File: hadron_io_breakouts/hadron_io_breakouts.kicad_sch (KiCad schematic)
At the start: 15 parts, among them J1 TF38-18S-0.5SV_830_, J2 SFM-110-02-L-D-A, J3 TF38-18S-0.5SV_830_, J4 SAMTEC-SFM-120-02-L-D-A, J5 SM04B-NSHSS-TB_LF__SN_, J6 SM08B-NSHSS-TB LFSN, J7 Conn_01x03_Pin

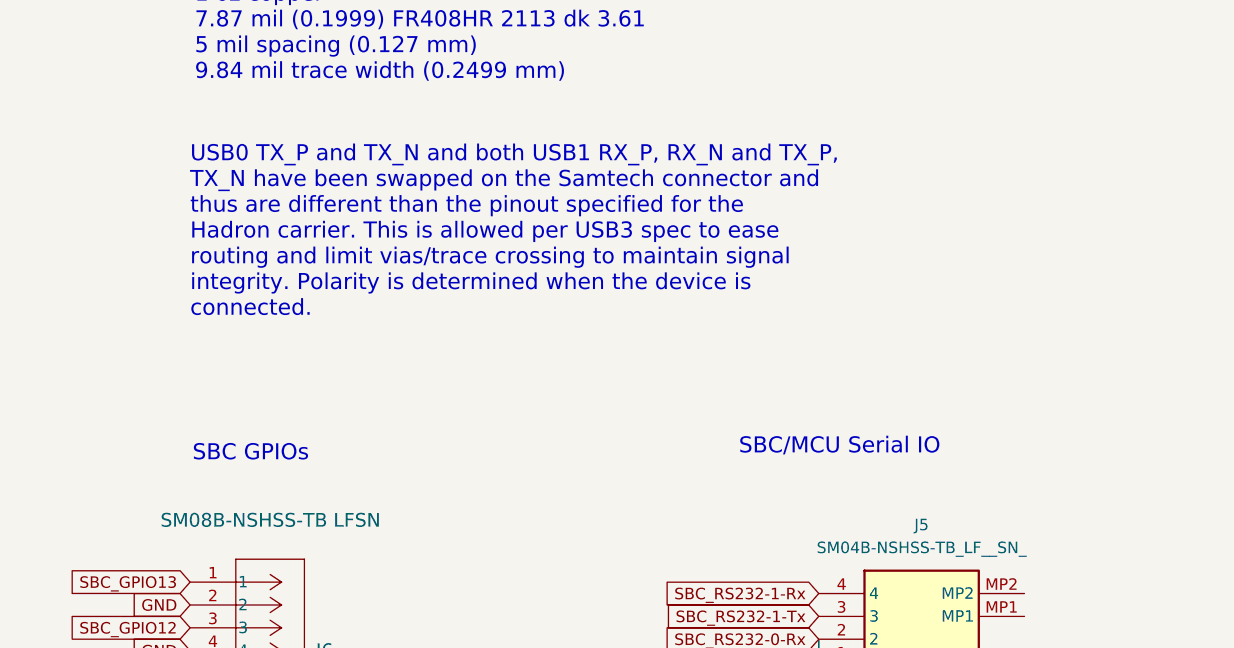
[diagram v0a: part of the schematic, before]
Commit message: added external trigger code to CamtrawlControl.ino
Minor cleanup of hadron_io_breakouts. Removed 6 layer version of the breakout.
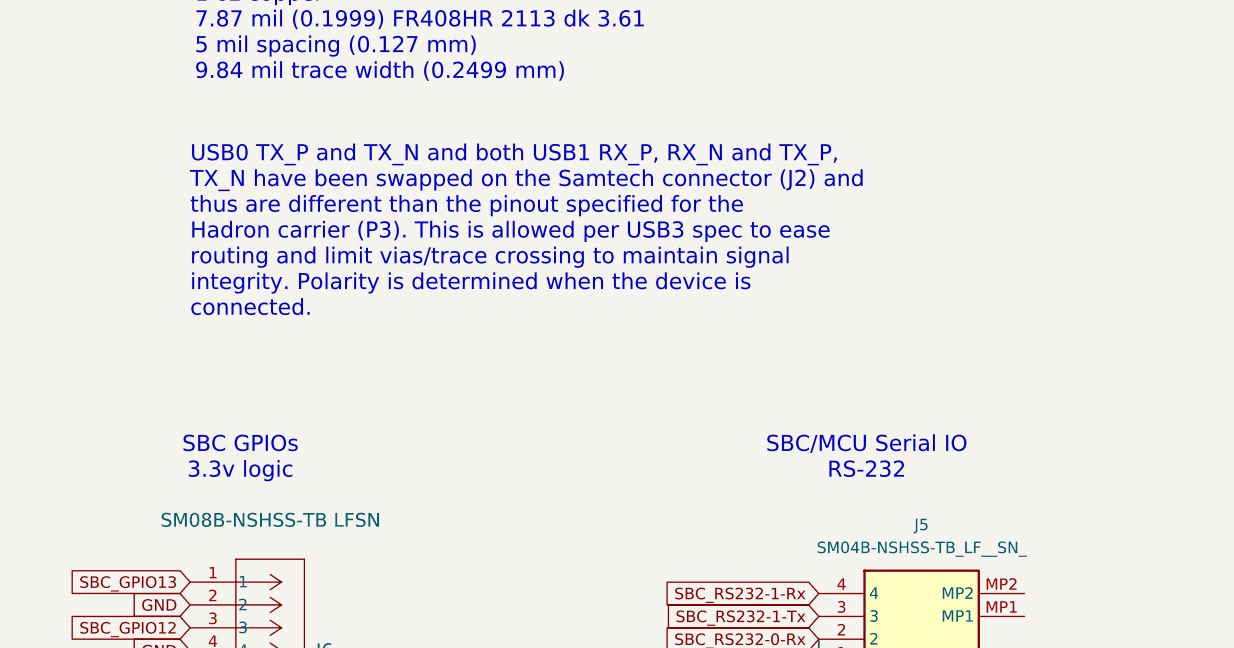
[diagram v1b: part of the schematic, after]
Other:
- note added: "SBC GPIOs 3.3v logic"
- note added: "SBC/MCU Serial IO RS-232"
- note added: "USB0 TX_P and TX_N and both USB1 RX_P, RX_N and TX_P, TX_N have been swapped on the Samtech connector (J2) and thus are different than the pinout specified for the Hadron carrier (P3). This is allowed per USB3 spec to ease routing and limit vias/trace crossing to maintain signal integrity. Polarity is determined when the device is connected."
- note removed: "SBC GPIOs"
- note removed: "SBC/MCU Serial IO"
- note removed: "USB0 TX_P and TX_N and both USB1 RX_P, RX_N and TX_P, TX_N have been swapped on the Samtech connector and thus are different than the pinout specified for the Hadron carrier. This is allowed per USB3 spec to ease routing and limit vias/trace crossing to maintain signal integrity. Polarity is determined when the device is connected."
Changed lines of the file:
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@@
 		)
 	)
-	(text "SBC GPIOs"
+	(text "SBC GPIOs\n3.3v logic"
 		(exclude_from_sim no)
-		(at 48.514 145.796 0)
+		(at 53.848 146.304 0)
 		(effects
 			(font
 				(size 1.778 1.778)
 			)
-			(justify left)
 		)
 	)
@@
 		)
 	)
-	(text "SBC/MCU Serial IO"
+	(text "SBC/MCU Serial IO\nRS-232\n"
 		(exclude_from_sim no)
-		(at 109.22 145.034 0)
+		(at 123.444 146.304 0)
 		(effects
 			(font
 				(size 1.778 1.778)
 			)
-			(justify left)
 		)
 	)
-	(text "USB0 TX_P and TX_N and both USB1 RX_P, RX_N and TX_P,\nTX_N have been swapped on the Samtech connector and\nthus are different than the pinout specified for the\nHadron carrier. This is allowed per USB3 spec to ease\nrouting and limit vias/trace crossing to maintain signal\nintegrity. Polarity is determined when the device is\nconnected."
+	(text "USB0 TX_P and TX_N and both USB1 RX_P, RX_N and TX_P,\nTX_N have been swapped on the Samtech connector (J2) and\nthus are different than the pinout specified for the\nHadron carrier (P3). This is allowed per USB3 spec to ease\nrouting and limit vias/trace crossing to maintain signal\nintegrity. Polarity is determined when the device is\nconnected."
 		(exclude_from_sim no)
 		(at 48.26 121.158 0)

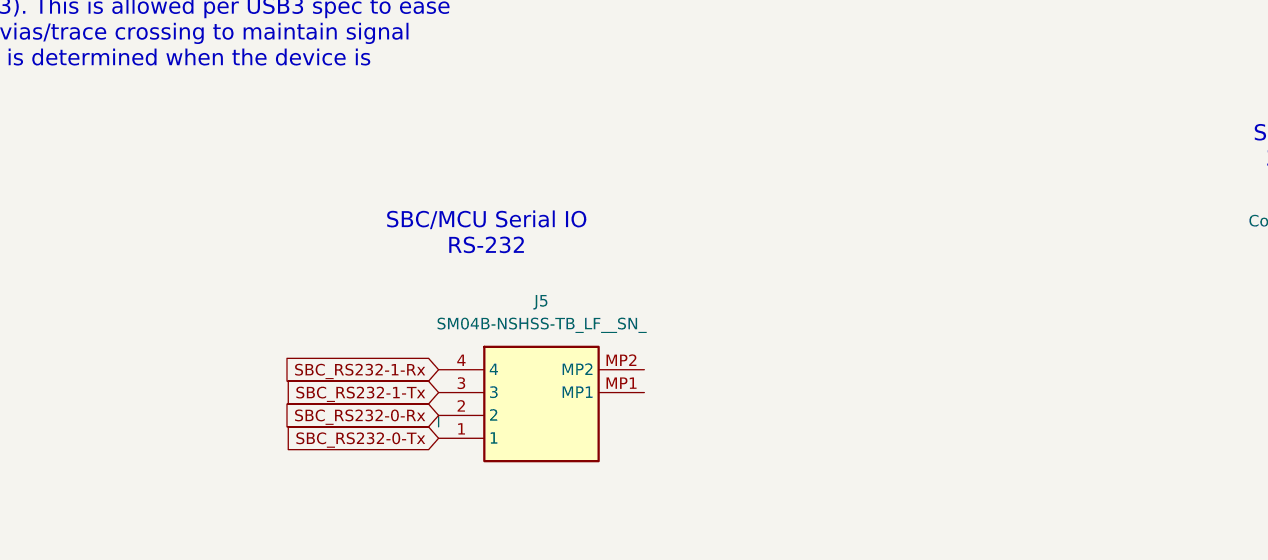
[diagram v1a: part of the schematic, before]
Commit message: Added note about change in tty assignment
In Jetpack 6.2.2 RS-232 interfaces are assigned different device IDs which are not consistent with the Hadron manual.
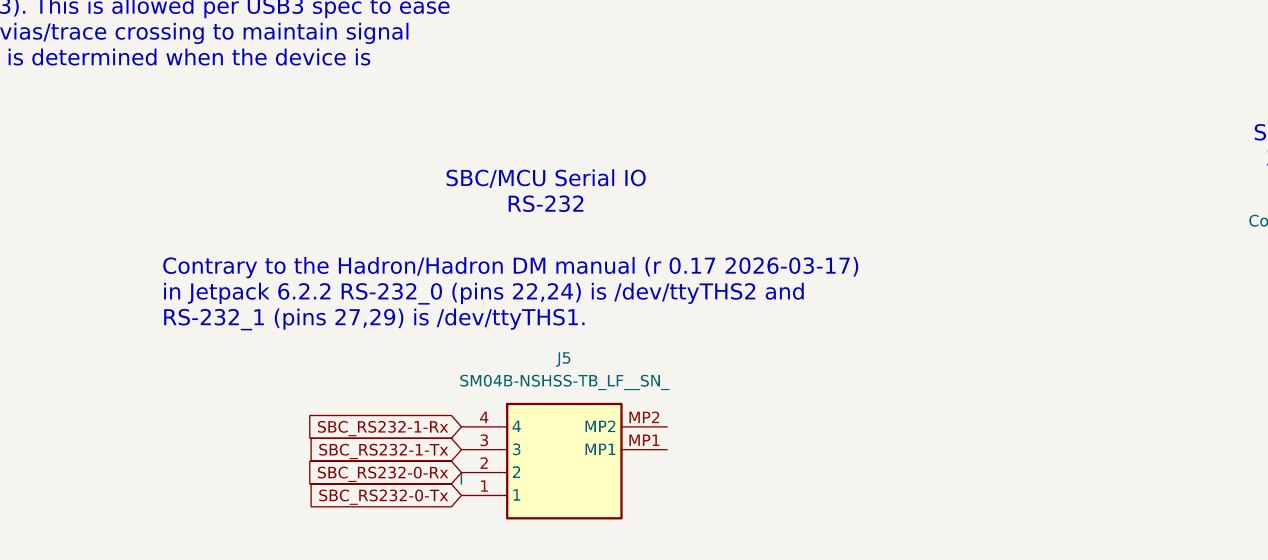
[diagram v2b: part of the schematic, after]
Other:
- note added: "Contrary to the Hadron/Hadron DM manual (r 0.17 2026-03-17) in Jetpack 6.2.2 RS-232_0 (pins 22,24) is /dev/ttyTHS2 and RS-232_1 (pins 27,29) is /dev/ttyTHS1."
- moved on the sheet: J5
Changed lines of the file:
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@@
 		)
 	)
+	(text "Contrary to the Hadron/Hadron DM manual (r 0.17 2026-03-17)\nin Jetpack 6.2.2 RS-232_0 (pins 22,24) is /dev/ttyTHS2 and\nRS-232_1 (pins 27,29) is /dev/ttyTHS1."
+		(exclude_from_sim no)
+		(at 87.376 152.908 0)
+		(effects
+			(font
+				(size 1.778 1.778)
+			)
+			(justify left)
+		)
+	)
 	(text "USB3 to TF38\nFor Flir Board Level Camera Integration"
 		(exclude_from_sim no)
@@
 	(text "SBC/MCU Serial IO\nRS-232\n"
 		(exclude_from_sim no)
-		(at 123.444 146.304 0)
+		(at 130.048 141.732 0)
 		(effects
 			(font
@@
 	(wire
 		(pts
-			(xy 118.11 167.64) (xy 118.11 166.37)
+			(xy 120.65 173.99) (xy 120.65 172.72)
 		)
 		(stroke
@@
 	(global_label "SBC_RS232-1-Tx"
 		(shape input)
-		(at 118.11 163.83 180)
+		(at 120.65 170.18 180)
 		(fields_autoplaced yes)
 		(effects
@@
 		)
 		(property "Intersheetrefs" "${INTERSHEET_REFS}"
-			(at 97.9497 163.83 0)
+			(at 100.4897 170.18 0)
 			(effects
 				(font
@@
 	(global_label "SBC_RS232-0-Tx"
 		(shape input)
-		(at 118.11 168.91 180)
+		(at 120.65 175.26 180)
 		(fields_autoplaced yes)
 		(effects
@@
 		)
 		(property "Intersheetrefs" "${INTERSHEET_REFS}"
-			(at 97.9497 168.91 0)
+			(at 100.4897 175.26 0)
 			(effects
 				(font
@@
 	(global_label "SBC_RS232-1-Rx"
 		(shape input)
-		(at 118.11 161.29 180)
+		(at 120.65 167.64 180)
 		(fields_autoplaced yes)
 		(effects
@@
 		)
 		(property "Intersheetrefs" "${INTERSHEET_REFS}"
-			(at 97.6473 161.29 0)
+			(at 100.1873 167.64 0)
 			(effects
 				(font
@@
 	(global_label "SBC_RS232-0-Rx"
 		(shape input)
-		(at 118.11 166.37 180)
+		(at 120.65 172.72 180)
 		(fields_autoplaced yes)
 		(effects
@@
 		)
 		(property "Intersheetrefs" "${INTERSHEET_REFS}"
-			(at 97.6473 166.37 0)
+			(at 100.1873 172.72 0)
 			(effects
 				(font
@@
 	(symbol
 		(lib_id "Ricks_symbols:SM04B-NSHSS-TB_LF__SN_")
-		(at 118.11 161.29 0)
+		(at 120.65 167.64 0)
 		(unit 1)
 		(exclude_from_sim no)
@@
 		(fields_autoplaced yes)
 		(property "Reference" "J5"
-			(at 129.54 153.67 0)
+			(at 132.08 160.02 0)
 			(effects
 				(font
@@
 		)
 		(property "Value" "SM04B-NSHSS-TB_LF__SN_"
-			(at 129.54 156.21 0)
+			(at 132.08 162.56 0)
 			(effects
 				(font
@@
 		)
 		(property "Footprint" "Ricks_Library:CONN_JST_SM04B-NSHSS-TB"
-			(at 137.16 256.21 0)
+			(at 139.7 262.56 0)
 			(effects
 				(font
@@
 		)
 		(property "Datasheet" "http://www.jst-mfg.com/product/pdf/eng/eNSH.pdf"
-			(at 137.16 356.21 0)
+			(at 139.7 362.56 0)
 			(effects
 				(font
@@
 		)
 		(property "Description" "JST NSH Series, 1mm Pitch 4 Way 1 Row Right Angle PCB Header, Solder Termination, 10A"
-			(at 132.588 177.546 0)
+			(at 135.128 183.896 0)
 			(effects
 				(font
@@
 		)
 		(property "Height" "4.4"
-			(at 137.16 556.21 0)
+			(at 139.7 562.56 0)
 			(effects
 				(font
@@
 		)
 		(property "Mouser Part Number" ""
-			(at 137.16 656.21 0)
+			(at 139.7 662.56 0)
 			(effects
 				(font
@@
 		)
 		(property "Mouser Price/Stock" ""
-			(at 137.16 756.21 0)
+			(at 139.7 762.56 0)
 			(effects
 				(font
@@
 		)
 		(property "Manufacturer_Name" "JST (JAPAN SOLDERLESS TERMINALS)"
-			(at 137.16 856.21 0)
+			(at 139.7 862.56 0)
 			(effects
 				(font
@@
 		)
 		(property "Manufacturer_Part_Number" "SM04B-NSHSS-TB(LF)(SN)"
-			(at 137.16 956.21 0)
+			(at 139.7 962.56 0)
 			(effects
 				(font
